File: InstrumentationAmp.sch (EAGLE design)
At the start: 14 parts, among them IC1 AD623R

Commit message: Names match README; connect Vref
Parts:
- SENSOR: device SparkFun-Connectors:CONN_02 -> SparkFun-Connectors:CONN_03
- renumbered JP_VNEG to JP_VC-
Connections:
- removed net N$3: IC1.REF, JP_REF.2
- removed net VIN+: IC1.+, SENSOR.2
- removed net VIN-: IC1.-, JP_VIN-.2, SENSOR.1
- new net VREF: IC1.REF, JP_REF.2, SENSOR.1
- new net VS+: IC1.+, SENSOR.3
- new net VS-: IC1.-, JP_VIN-.2, SENSOR.2
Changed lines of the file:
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@@
 <part name="SUPPLY14" library="SparkFun-PowerSymbols" deviceset="VNEG" device=""/>
 <part name="SUPPLY15" library="supply2" deviceset="GND" device=""/>
-<part name="JP_VNEG" library="SparkFun-Jumpers" deviceset="JUMPER-SMT_2_NC_PASTE" device="_SILK" value=""/>
+<part name="JP_VC-" library="SparkFun-Jumpers" deviceset="JUMPER-SMT_2_NC_PASTE" device="_SILK" value=""/>
 <part name="SUPPLY2" library="SparkFun-PowerSymbols" deviceset="VCC" device=""/>
 <part name="SUPPLY3" library="supply2" deviceset="GND" device=""/>
@@
 <part name="SUPPLY5" library="SparkFun-PowerSymbols" deviceset="VOUT" device=""/>
 <part name="LOGGER" library="SparkFun-Connectors" deviceset="CONN_04" device=""/>
-<part name="SENSOR" library="SparkFun-Connectors" deviceset="CONN_02" device=""/>
+<part name="SENSOR" library="SparkFun-Connectors" deviceset="CONN_03" device=""/>
 </parts>
 <sheets>
 <sheet>
 <plain>
-<text x="2.54" y="-30.48" size="1.778" layer="97">2.7-12.0 V</text>
+<text x="2.54" y="-27.94" size="1.778" layer="97">2.7-12.0 V</text>
 </plain>
 <instances>
@@
 <instance part="CFP1" gate="G$1" x="-10.16" y="-40.64" rot="R90"/>
 <instance part="SUPPLY7" gate="GND" x="15.24" y="-45.72"/>
-<instance part="SUPPLY8" gate="G$1" x="-2.54" y="-33.02"/>
+<instance part="SUPPLY8" gate="G$1" x="-2.54" y="-27.94"/>
 <instance part="SUPPLY9" gate="GND" x="17.78" y="-96.52"/>
 <instance part="SUPPLY10" gate="GND" x="-20.32" y="-93.98"/>
@@
 <instance part="SUPPLY14" gate="G$2" x="-2.54" y="-114.3" rot="R180"/>
 <instance part="SUPPLY15" gate="GND" x="-2.54" y="-134.62"/>
-<instance part="JP_VNEG" gate="G$1" x="-2.54" y="-124.46" rot="R90"/>
+<instance part="JP_VC-" gate="G$1" x="-2.54" y="-124.46" rot="R90"/>
 <instance part="SUPPLY2" gate="G$1" x="-7.62" y="40.64"/>
 <instance part="SUPPLY3" gate="GND" x="7.62" y="30.48"/>
@@
 <instance part="SUPPLY5" gate="G$1" x="12.7" y="20.32" rot="R270"/>
 <instance part="LOGGER" gate="G$1" x="-25.4" y="33.02"/>
-<instance part="SENSOR" gate="G$1" x="-27.94" y="50.8"/>
+<instance part="SENSOR" gate="J$1" x="-27.94" y="60.96"/>
 </instances>
 <busses>
@@
 <segment>
 <pinref part="SUPPLY15" gate="GND" pin="GND"/>
-<pinref part="JP_VNEG" gate="G$1" pin="1"/>
+<pinref part="JP_VC-" gate="G$1" pin="1"/>
 <wire x1="-2.54" y1="-132.08" x2="-2.54" y2="-129.54" width="0.1524" layer="91"/>
 </segment>
@@
 <wire x1="-2.54" y1="-40.64" x2="-7.62" y2="-40.64" width="0.1524" layer="91"/>
 <junction x="-2.54" y="-40.64"/>
-<wire x1="-2.54" y1="-40.64" x2="-2.54" y2="-33.02" width="0.1524" layer="91"/>
+<wire x1="-2.54" y1="-40.64" x2="-2.54" y2="-27.94" width="0.1524" layer="91"/>
 <pinref part="SUPPLY8" gate="G$1" pin="VCC"/>
 </segment>
@@
 </segment>
 </net>
-<net name="VIN+" class="0">
+<net name="VS+" class="0">
 <segment>
 <pinref part="IC1" gate="G$1" pin="+"/>
@@
 </segment>
 <segment>
-<wire x1="-20.32" y1="53.34" x2="-10.16" y2="53.34" width="0.1524" layer="91"/>
-<label x="-17.78" y="53.34" size="1.778" layer="95"/>
-<pinref part="SENSOR" gate="G$1" pin="2"/>
+<wire x1="-20.32" y1="63.5" x2="-10.16" y2="63.5" width="0.1524" layer="91"/>
+<label x="-17.78" y="63.5" size="1.778" layer="95"/>
+<pinref part="SENSOR" gate="J$1" pin="3"/>
 </segment>
 </net>
@@
 <segment>
 <pinref part="SUPPLY14" gate="G$2" pin="VNEG"/>
-<pinref part="JP_VNEG" gate="G$1" pin="2"/>
+<pinref part="JP_VC-" gate="G$1" pin="2"/>
 <wire x1="-2.54" y1="-119.38" x2="-2.54" y2="-116.84" width="0.1524" layer="91"/>
 </segment>
@@
 </segment>
 </net>
-<net name="VIN-" class="0">
+<net name="VS-" class="0">
 <segment>
 <pinref part="IC1" gate="G$1" pin="-"/>
@@
 </segment>
 <segment>
-<wire x1="-20.32" y1="50.8" x2="-10.16" y2="50.8" width="0.1524" layer="91"/>
-<label x="-17.78" y="50.8" size="1.778" layer="95"/>
-<pinref part="SENSOR" gate="G$1" pin="1"/>
-</segment>
-</net>
-<net name="N$3" class="0">
+<wire x1="-20.32" y1="60.96" x2="-10.16" y2="60.96" width="0.1524" layer="91"/>
+<label x="-17.78" y="60.96" size="1.778" layer="95"/>
+<pinref part="SENSOR" gate="J$1" pin="2"/>
+</segment>
+</net>
+<net name="VREF" class="0">
 <segment>
 <pinref part="IC1" gate="G$1" pin="REF"/>
@@
 <pinref part="JP_REF" gate="G$1" pin="2"/>
 <wire x1="17.78" y1="-78.74" x2="17.78" y2="-81.28" width="0.1524" layer="91"/>
-</segment>
-</net>
+<label x="5.08" y="-78.74" size="1.778" layer="95"/>
+</segment>
+<segment>
+<pinref part="SENSOR" gate="J$1" pin="1"/>
+<wire x1="-20.32" y1="58.42" x2="-10.16" y2="58.42" width="0.1524" layer="91"/>
+<label x="-17.78" y="58.42" size="1.778" layer="95"/>
+</segment>
+</net>

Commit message: ERC, DRC
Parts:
- renumbered JP_VIN- to JP_VS-
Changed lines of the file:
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@@
 <part name="RG4" library="resistor" deviceset="R-US_" device="0207/10"/>
 <part name="SUPPLY11" library="SparkFun-PowerSymbols" deviceset="VNEG" device=""/>
-<part name="JP_VIN-" library="SparkFun-Jumpers" deviceset="JUMPER-SMT_2_NC_PASTE" device="_SILK" value=""/>
+<part name="JP_VS-" library="SparkFun-Jumpers" deviceset="JUMPER-SMT_2_NC_PASTE" device="_SILK" value=""/>
 <part name="CFN1" library="SparkFun-Capacitors" deviceset="0.1UF" device="-0603-25V-(+80/-20%)" value="0.1uF"/>
 <part name="CFN10" library="SparkFun-Capacitors" deviceset="10UF" device="-0603-6.3V-20%" value="10uF"/>
@@
 <instance part="RG4" gate="G$1" x="-20.32" y="-66.04" rot="R90"/>
 <instance part="SUPPLY11" gate="G$2" x="-2.54" y="-88.9"/>
-<instance part="JP_VIN-" gate="G$1" x="-20.32" y="-83.82" rot="R90"/>
+<instance part="JP_VS-" gate="G$1" x="-20.32" y="-83.82" rot="R90"/>
 <instance part="CFN1" gate="G$1" x="-10.16" y="-99.06"/>
 <instance part="CFN10" gate="G$1" x="5.08" y="-99.06"/>
@@
 </segment>
 <segment>
-<pinref part="JP_VIN-" gate="G$1" pin="1"/>
+<pinref part="JP_VS-" gate="G$1" pin="1"/>
 <pinref part="SUPPLY10" gate="GND" pin="GND"/>
 <wire x1="-20.32" y1="-91.44" x2="-20.32" y2="-88.9" width="0.1524" layer="91"/>
@@
 <pinref part="IC1" gate="G$1" pin="-"/>
 <wire x1="-10.16" y1="-76.2" x2="-20.32" y2="-76.2" width="0.1524" layer="91"/>
-<pinref part="JP_VIN-" gate="G$1" pin="2"/>
+<pinref part="JP_VS-" gate="G$1" pin="2"/>
 <wire x1="-20.32" y1="-76.2" x2="-20.32" y2="-78.74" width="0.1524" layer="91"/>
 <label x="-15.24" y="-76.2" size="1.778" layer="95"/>

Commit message: Initial layout of Amp 2.0
Changed schematic to add on board buck-boost converter, mux to control gain, and I2C IO expander to allow gain to be controlled via I2C. Preliminary layout complete, ready for verification
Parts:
- removed RG1, RG2, RG3, RG4: (no value), resistor:R-US_0207/10
- added C1: 0.1uF, rcl:C-EUC0603
- added C2, C7: 10uF, rcl:C-EUC0603
- added C3: 10pF, rcl:C-EUC0603
- added C5: 22uF, rcl:C-EUC0603
- added D1: GREEN, SparkFun-LED:LED-GREEN0603
- added D2: BLUE, SparkFun-LED:LED-BLUE0603
- added J1: (no value), SparkFun-Connectors:I2C_STANDARD
- added Q1, Q2: 310mA/60V/1.6Ω, SparkFun-DiscreteSemi:MOSFET-NCH-2N7002PW
- added R10, R11, R12, R14, R15, R16, R17, R18, R19, R5, R6, R7, R8, R9: (no value), rcl:R-EU_R0603
- added R13, R2, R3, R4: 10k, rcl:R-EU_R0603
- added R20: 143k, rcl:R-EU_R0603
- added R21: 953k, rcl:R-EU_R0603
- added S1: 219-03, switch-dil:219-03
- added U$1: MAX4638, Custom:MAX4638
- added U$2: TCA9534A, Custom:TCA9534A
- added U$3, U$4, U$5: FDN358P, Custom:FDN358P
- added U$6: MIC842, Custom:MIC842
- added U$7: TPS63061, Custom:TPS306X
- added U$8: 1uH, Custom:WE-MAIA(INDUCTOR)
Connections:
- removed net RG-A: IC1.RG@1, RG1.2, RG2.2, RG3.2, RG4.2
- removed net RG-B: IC1.RG@2, RG1.1, RG2.1, RG3.1, RG4.1
- new net 5V: C5.1, D2.A, R18.2, R19.2, R21.2, S1.4, S1.5, S1.6, U$1.EN, U$1.V+, U$2.VCC, U$6.VDD, U$7.VOUT
- new net INT: U$2./INT
- new net N$1: U$7.L2, U$8.2
- new net N$11: R7.2, U$1.NO3
- new net N$12: R8.2, U$1.NO4
- new net N$13: R9.2, U$1.NO5
- new net N$14: R10.2, U$1.NO6
- new net N$15: R11.2, U$1.NO7
- new net N$16: R12.2, U$1.NO8
- new net N$17: D1.C, R15.1
- new net N$18: D1.A, R14.1, U$6.OUT
- new net N$19: C3.1, R20.2, R21.1, U$7.FB
- new net N$2: U$7.L1, U$8.1
- new net N$3: D2.C, R14.2
- new net N$4: S1.2, U$4.D
- new net N$5: C1.1, U$7.VAUX
- new net N$6: S1.3, U$5.D
- new net N$7: S1.1, U$3.D
- new net N$8: R5.2, U$1.NO1
- new net N$9: R6.2, U$1.NO2
- new net R_GAIN+: IC1.RG@1, U$1.COM
- new net R_GAIN-: IC1.RG@2, R10.1, R11.1, R12.1, R5.1, R6.1, R7.1, R8.1, R9.1
- new net S1: R4.2, U$1.A0, U$2.P1, U$5.S
- new net S2: R2.2, U$1.A1, U$2.P2, U$4.S
- new net S3: R3.2, U$1.A2, U$2.P3, U$3.S
- new net SCL: Q2.D, R19.1, U$2.SCL
- new net SCL_OUT: J1.4, Q2.S, R17.1
- new net SDA: Q1.D, R18.1, U$2.SDA
- new net SDA_OUT: J1.3, Q1.S, R16.1
- new net SW_G: R13.2, U$2.P0, U$3.G, U$4.G, U$5.G, U$6.INP
- new net V_LOGIC: J1.2, Q1.G, Q2.G, R16.2, R17.2
- net GND: now also C1.2, C2.2, C3.2, C5.2, C7.2, J1.1, R13.1, R15.2, R2.1, R20.1, R3.1, R4.1, U$1.GND@1, U$1.GND@2, U$1.V-, U$2.A0, U$2.A1, U$2.A2, U$2.GND, U$6.GND, U$7.GND, U$7.PGND, U$7.PS/SYNC
- net VCC: now also C2.1, C7.1, U$7.EN, U$7.VIN
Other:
- note added: "2.5v-12v"
- note added: "ADD RESISTOR DIVIDER, FIX VOLTAGE!"

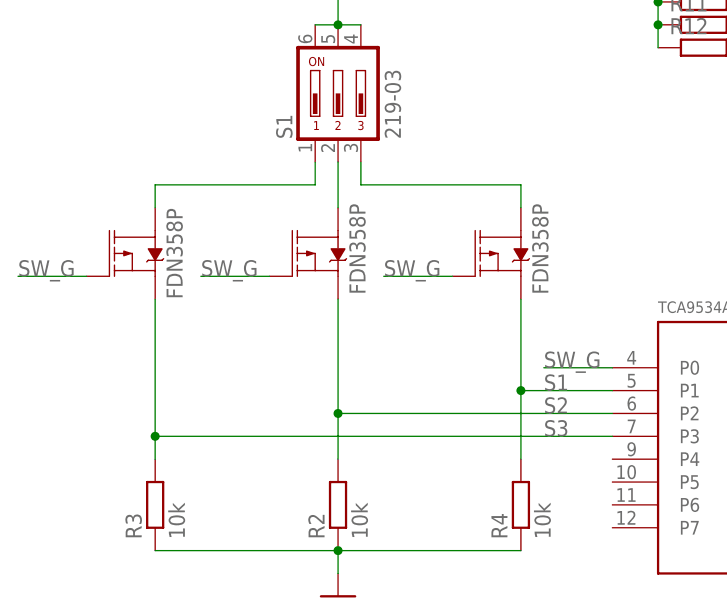
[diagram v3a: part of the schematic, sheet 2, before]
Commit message: Made Edits from 1st round of board testing
Flipped direciton of PFETs, fixed switch mode regulator package, changed capacitor sizes, chained set resistor values, etc. Verification still required that all changes are made
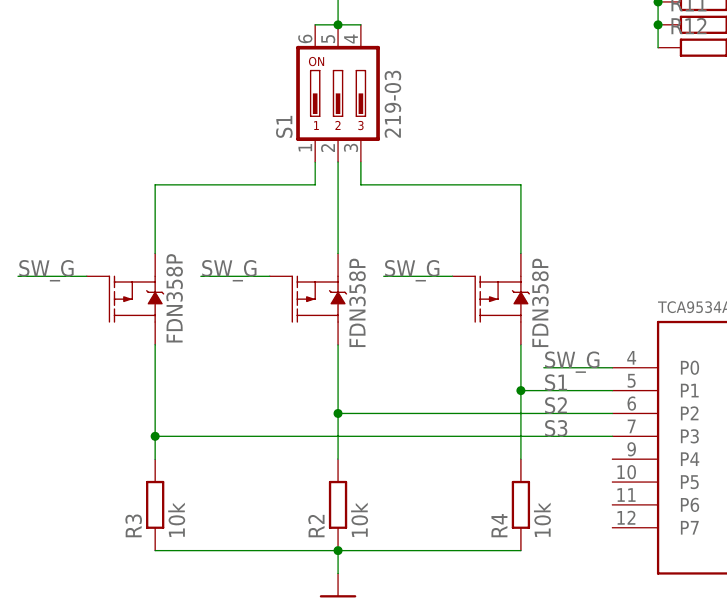
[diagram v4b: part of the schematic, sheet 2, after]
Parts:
- removed U$7: TPS63061, Custom:TPS306X
- added U1: (no value), bschulz:TPS63061
- C2, C7: device rcl:C-EUC0603 -> bschulz:C-EU10UFC0805
- C5: device rcl:C-EUC0603 -> bschulz:C-EU22UFC0805
- CFN10, CFP10: device SparkFun-Capacitors:10UF-0603-6.3V-20% -> bschulz:C-EUC0805
- R20: value 143k -> 111k
- R21: value 953k -> 1M
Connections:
- removed net N$2: U$7.L1, U$8.1
- removed net N$4: S1.2, U$4.D
- new net N$20: U$8.2, U1.L2
- new net N$23: C1.1, U1.VAUX
- net 5V: now also U1.VOUT; no longer U$7.VOUT
- net GND: now also U1.GND, U1.PGND, U1.PSYNC; no longer U$7.GND, U$7.PGND, U$7.PS/SYNC
- net N$1: now also S1.2, U$4.S; no longer U$7.L2, U$8.2
- net N$19: now also U1.FB; no longer U$7.FB
- net N$5: now also U$8.1, U1.L1; no longer C1.1, U$7.VAUX
- net N$6: now also U$5.S; no longer U$5.D
- net N$7: now also U$3.S; no longer U$3.D
- net S1: now also U$5.D; no longer U$5.S
- net S2: now also U$4.D; no longer U$4.S
- net S3: now also U$3.D; no longer U$3.S
- net VCC: now also U1.EN, U1.VIN; no longer U$7.EN, U$7.VIN
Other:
- moved on the sheet: CFN10, CFP10
